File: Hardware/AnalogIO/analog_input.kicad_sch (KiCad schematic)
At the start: 14 parts

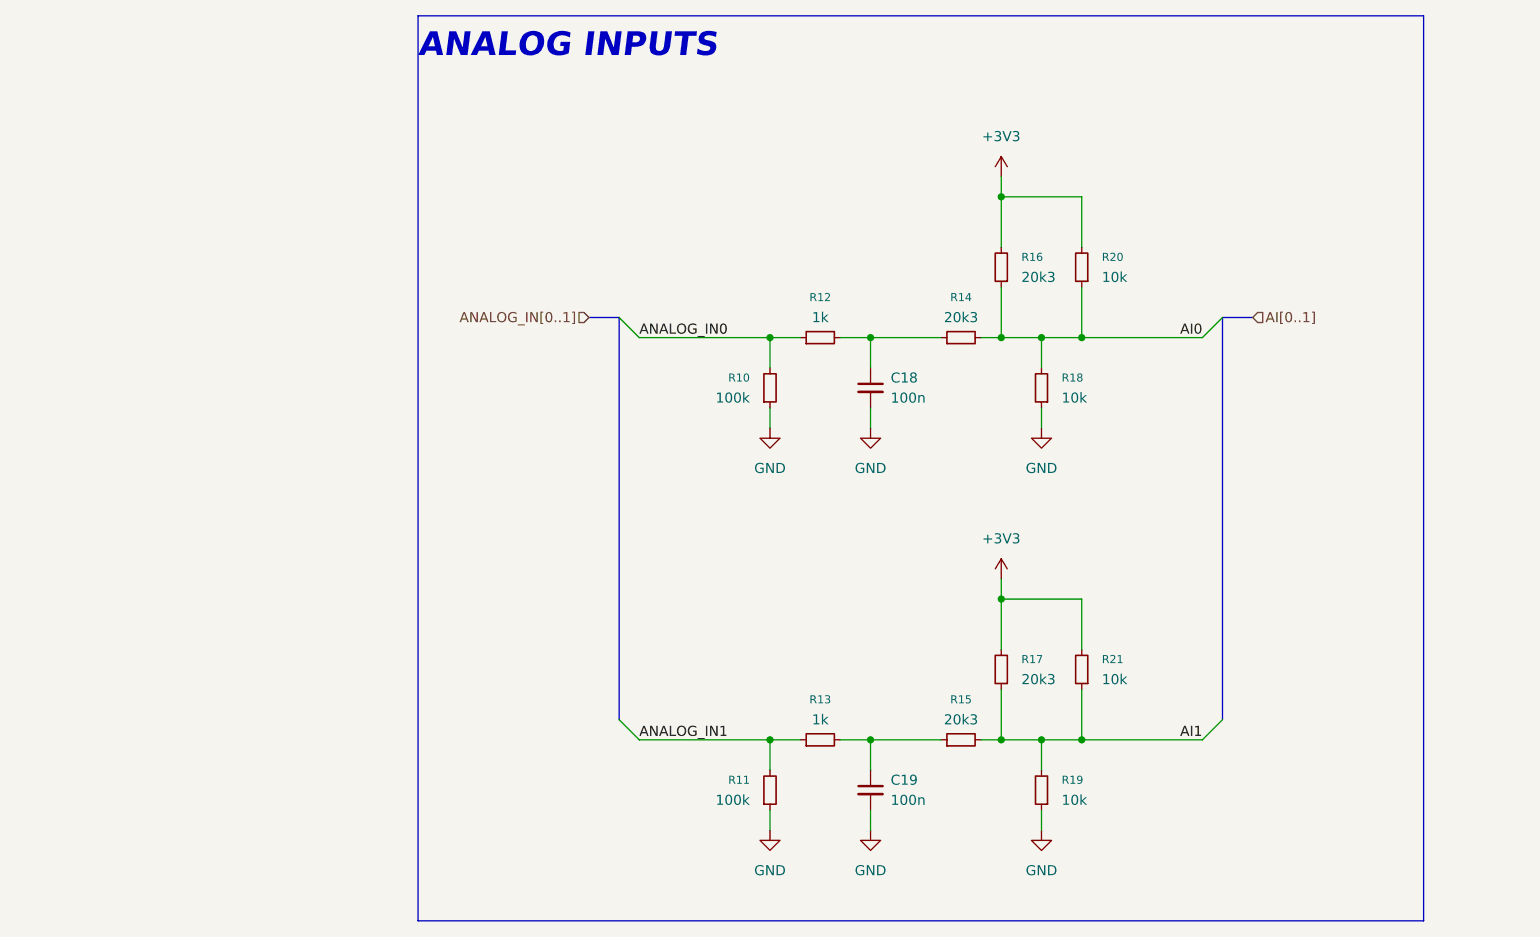
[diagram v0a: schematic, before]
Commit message: schematic update - all pcbs
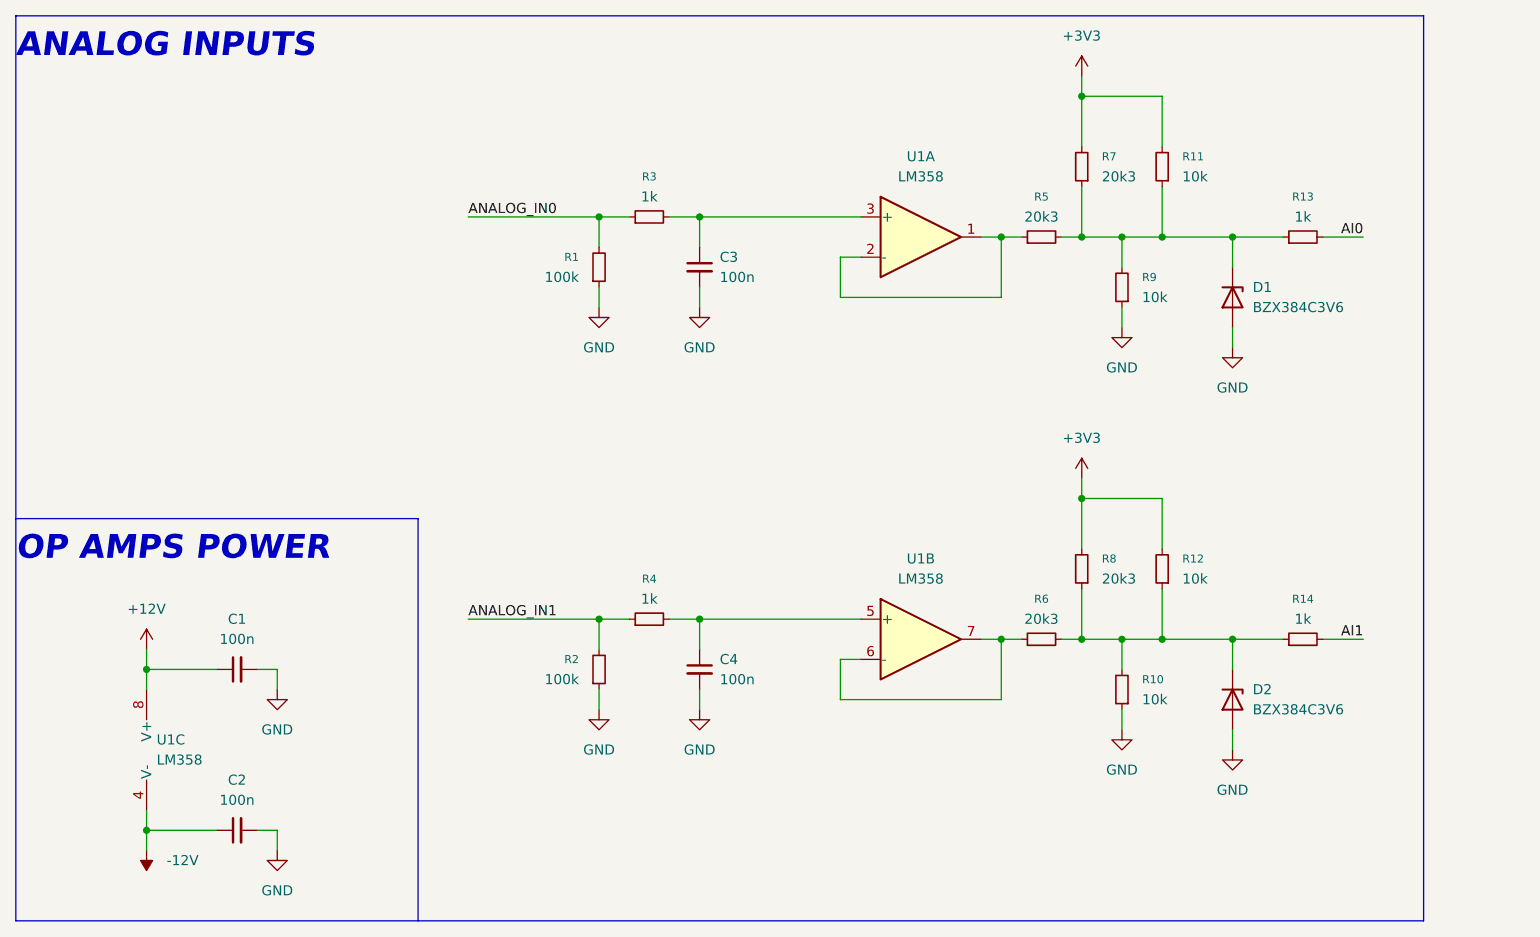
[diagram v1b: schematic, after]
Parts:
- added C1, C2: 100n, symbol Device:C_Small
- added D1, D2: BZX384C3V6, Diode_SMD:D_SOD-323, symbol Diode:BZX384xxxx
- added R13, R14: 1k, Resistor_SMD:R_0603_1608Metric_Pad0.98x0.95mm_HandSolder, symbol Device:R_Small
- added U1: LM358, symbol Amplifier_Operational:LM358
- renumbered C18 to C3, C19 to C4, R10 to R1, R19 to R10, R20 to R11, R21 to R12, R11 to R2, R12 to R3, R13 to R4, R14 to R5, R15 to R6, R16 to R7, R17 to R8, R18 to R9
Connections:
- net AI0: now also R13.2; no longer R11.1, R5.2, R7.1, R9.2
- net AI1: now also R14.2; no longer R10.2, R12.1, R6.2, R8.1
- net GND: now also C1.2, C2.2, D1.2 (A), D2.2 (A)
- net at C4.1, R4.2: now also U1.5 (+); no longer R6.1
- net at C3.1, R3.2: now also U1.3 (+); no longer R5.1
- new net: R6.1, U1.6 (-), U1.7
- new net: D2.1 (K), R10.2, R12.1, R14.1, R6.2, R8.1
- new net: D1.1 (K), R11.1, R13.1, R5.2, R7.1, R9.2
- new net: R5.1, U1.1, U1.2 (-)
- new net +12V: C1.1, U1.8 (V+)
- new net -12V: C2.1, U1.4 (V-)
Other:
- note added: "OP AMPS POWER"
- moved on the sheet: C3, C4, R1, R10, R11, R12, R2, R3, R4, R5, R6, R7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

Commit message: schematic update - digital and analog footprints added
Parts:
- added T1: AI0, TestPoint:TestPoint_Pad_1.0x1.0mm, symbol Connector:TestPoint_Small
- added T2: AI1, TestPoint:TestPoint_Pad_1.0x1.0mm, symbol Connector:TestPoint_Small
- C1, C2: footprint (none) -> Capacitor_SMD:C_0603_1608Metric_Pad1.08x0.95mm_HandSolder; Mouser Part Number (none) -> GRM033R6YA104ME14D; Mouser Price/Stock (none) -> https://www.mouser.pl/ProductDetail/Murata-Electronics/GRM0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
- R10, R11, R12, R9: Mouser Part Number 71-CRCW06031K00FKED -> 71-CRCW0603-10K-E3; Mouser Price/Stock https://www.mouser.pl/ProductDetail/Vishay-Dale/CRCW06031K0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 -> https://www.mouser.pl/ProductDetail/Vishay/CRCW060310K0FKEA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
- R5, R6, R7, R8: Mouser Part Number 71-CRCW06031K00FKED -> 71-CRCW0603-20.5K-E3; Mouser Price/Stock https://www.mouser.pl/ProductDetail/Vishay-Dale/CRCW06031K0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 -> https://www.mouser.pl/ProductDetail/Vishay/CRCW060320K5FKEA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
- U1: footprint (none) -> Package_SO:SOIC-8_3.9x4.9mm_P1.27mm; Mouser Part Number (none) -> 511-LM358D; Mouser Price/Stock (none) -> https://www.mouser.pl/ProductDetail/STMicroelectronics/LM35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
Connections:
- net OP_AI1_OUT: now reaches R6.1, U1.6 (-), U1.7
- net OP_AI1_OUT: now also T2.1
- net AI1_R1k: now reaches D2.1 (K), R10.2, R12.1, R14.1, R6.2, R8.1
- net AI0_R1k: now reaches D1.1 (K), R11.1, R13.1, R5.2, R7.1, R9.2
- net OP_AI0_OUT: now reaches R5.1, U1.1, U1.2 (-)
- net OP_AI0_OUT: now also T1.1
- net OP_AI0_IN: now reaches C3.1, R3.2, U1.3 (+)
- net OP_AI1_IN: now reaches C4.1, R4.2, U1.5 (+)
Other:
- moved on the sheet: D1, D2, R10, R11, R12, R13, R14, R5, R6, R7, R8, R9

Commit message: schematic update & pcb update
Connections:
- net +12V renamed +15V
- net -12V renamed -15V
- net AI0 renamed AI_0
- net AI1 renamed AI_1

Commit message: small adjustments and final revision
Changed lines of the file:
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@@
+	)
+	(junction
+		(at 71.12 120.65)
+		(diameter 0)
+		(color 0 0 0 0)
 	)
 	(junction
@@
 			)
 		)
+	)
+	(symbol
+		(lib_id "power:PWR_FLAG")
+		(at 71.12 120.65 270)
+		(unit 1)
+		(exclude_from_sim no)
+		(in_bom yes)
+		(on_board yes)
+		(dnp no)
+		(fields_autoplaced yes)
+		(property "Reference" "#FLG05"
+			(at 73.025 120.65 0)
+			(effects
+				(font
+					(size 1.27 1.27)
+				)
+				(hide yes)
+			)
+		)
+		(property "Value" "GND_FLAG"
+			(at 74.93 120.6499 90)
+			(effects
+				(font
+					(size 1.27 1.27)
+				)
+				(justify left)
+			)
+		)
+		(property "Footprint" ""
+			(at 71.12 120.65 0)
+			(effects
+				(font
+					(size 1.27 1.27)
+				)
+				(hide yes)
+			)
+		)
+		(property "Datasheet" "~"
+			(at 71.12 120.65 0)
+			(effects
+				(font
+					(size 1.27 1.27)
+				)
+				(hide yes)
+			)
+		)
+		(property "Description" "Special symbol for telling ERC where power comes from"
+			(at 71.12 120.65 0)
+			(effects
+				(font
+					(size 1.27 1.27)
+				)
+				(hide yes)
+			)
+		)
+		(pin "1"
+		)
+		(instances
+			(project ""
+				(path "/b652b05a-4e3d-4ad1-b032-18886abe7d45/c35516e2-6320-41b9-a032-9137d9aa80bb"
+					(reference "#FLG05")
+					(unit 1)
+				)
+			)
+		)
